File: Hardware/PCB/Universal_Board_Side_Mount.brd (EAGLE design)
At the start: 100.2 x 51 mm, 10 parts, among them U1 L7805CV

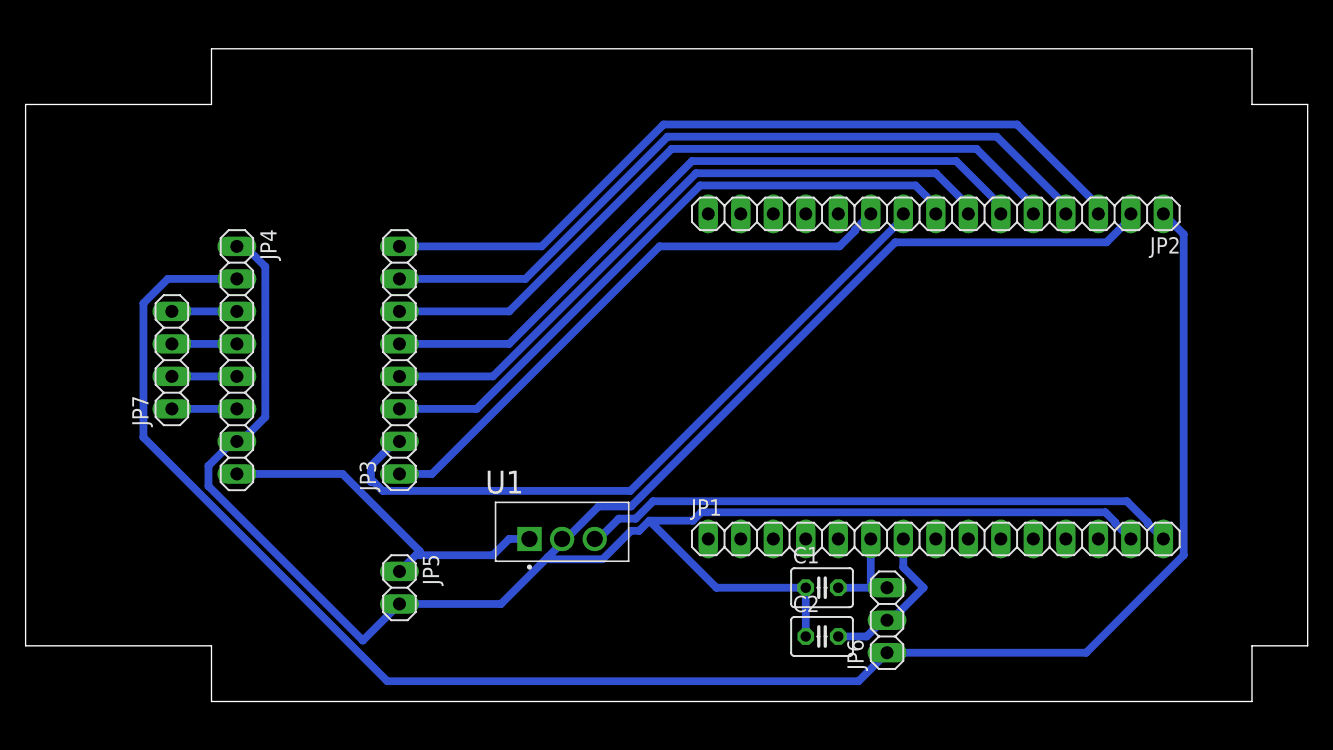
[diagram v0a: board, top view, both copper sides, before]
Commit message: Updated Side Board
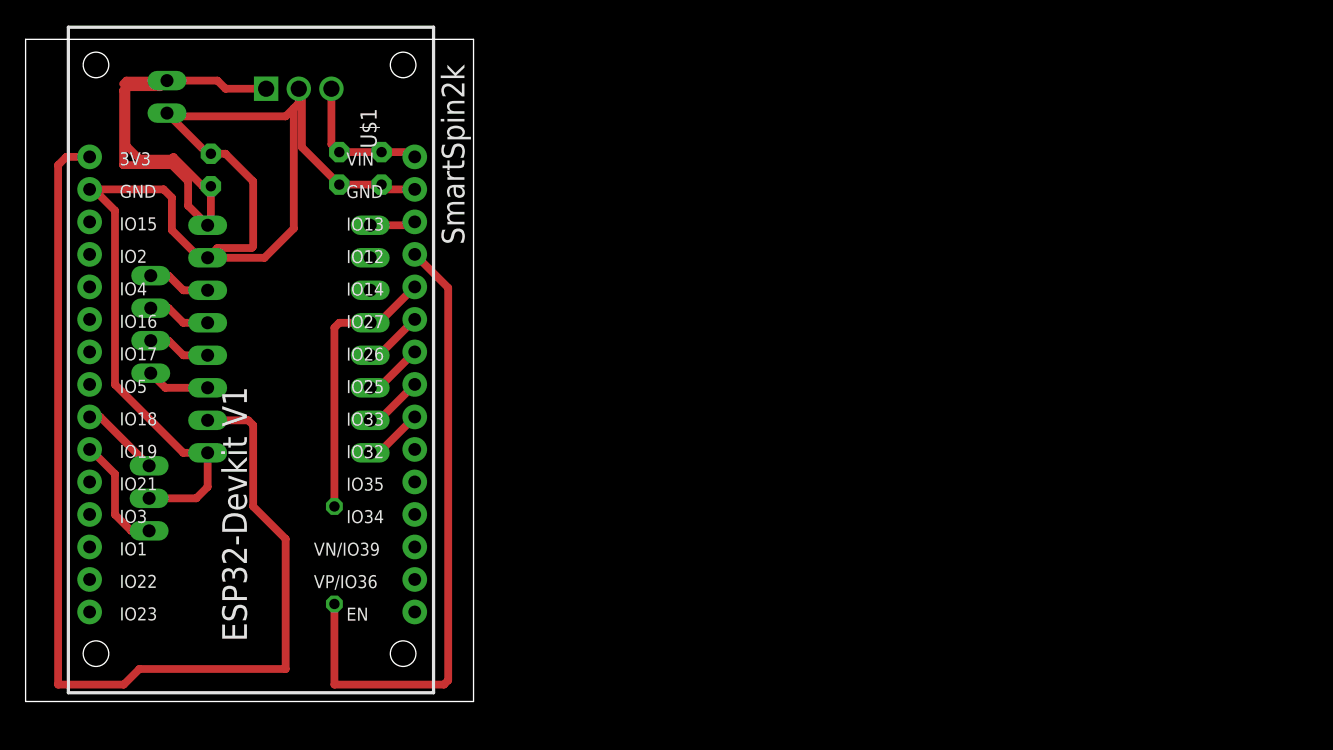
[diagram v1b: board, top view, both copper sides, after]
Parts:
- removed C1, C2: (no value), rcl:C025-030X050
- removed JP1, JP2: (no value), pinhead:1X15
- added C3: 100nf, capacitor-wima:C2.5-3
- added C4: 10uf, capacitor-wima:C2.5-3
- added C5: 100uf, capacitor-wima:C2.5-3
- added R1: 1k, rcl:0204/7
- added U$1: ESP32DEVKITV1, ESP32-DEVKITV1:ESP32-DEVKITV1
- moved JP6 58.4 mm to (9.65, 15.9), flipped to the bottom, turned to 270 degrees
- moved JP5 42.4 mm to (11.0, 47.2), flipped to the bottom
- moved U1 40.8 mm to (18.8, 47.9), flipped to the bottom, turned to 180 degrees
- moved JP7 3.25 mm to (9.78, 29.5), flipped to the bottom, turned to 270 degrees
- moved JP3 2.82 mm to (26.9, 28.3), flipped to the bottom, turned to 270 degrees
- moved JP4 2.82 mm to (14.2, 28.3), flipped to the bottom, turned to 90 degrees
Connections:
- removed net N$12: JP2.5, JP3.6
- removed net N$14: JP2.3, JP3.8
- new net N$15: JP6.1, U$1.D18
- net +12V: now also C5.1
- net +3V3: now also U$1.3V3; no longer JP2.1, JP6.1
- net +5V: now also C3.1, C4.1, U$1.VIN; no longer JP1.15
- net GND: now also C3.2, C4.2, C5.2, JP6.2, U$1.GND@1, U$1.GND@2; no longer C1.1, C2.1, JP1.14, JP2.2
- net N$1: now also JP3.4, R1.2, U$1.D14; no longer C2.2, JP1.7, JP6.2
- net N$13: now also JP6.3, U$1.D19; no longer JP2.4, JP3.7
- net N$2: now also JP3.1, U$1.D13; no longer C1.2, JP1.6, JP6.3
- net N$3: now also R1.1, U$1.D12; no longer JP2.10, JP3.1
- net N$4: now also JP3.5, U$1.D27; no longer JP2.8, JP3.3
- net N$5: now also JP3.6, U$1.D26; no longer JP2.7, JP3.4
- net N$6: now also JP3.7, U$1.D25; no longer JP2.6, JP3.5
- net N$7: now also JP3.8, U$1.D33; no longer JP2.9, JP3.2
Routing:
- net GND: track 181.1 -> 108.3 mm
- net N$14: track 62.1 -> 0.00 mm
- net N$12: track 57.5 -> 0.00 mm
- net +3V3: track 139.1 -> 85.4 mm
- net N$7: track 55.3 -> 4.64 mm
- net N$13: track 59.8 -> 9.14 mm
- net N$6: track 55.3 -> 4.64 mm
- net N$5: track 53.0 -> 4.64 mm
- net N$4: track 50.7 -> 4.64 mm
- net +5V: track 47.9 -> 11.3 mm
- net +12V: track 28.4 -> 46.5 mm
- net N$1: track 12.7 -> 21.6 mm
- net N$15: track 0.00 -> 6.23 mm
- net N$3: track 45.3 -> 49.7 mm
- net N$2: track 7.62 -> 3.59 mm
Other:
- board size 100.2 x 51 mm -> 35 x 51.7 mm
- board text added: "SmartSpin2k"
- board text added: "SmartSpin2k v1"
